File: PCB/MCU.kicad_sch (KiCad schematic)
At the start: 15 parts, among them U1 STM32G431CBT6, Y1 8MHz

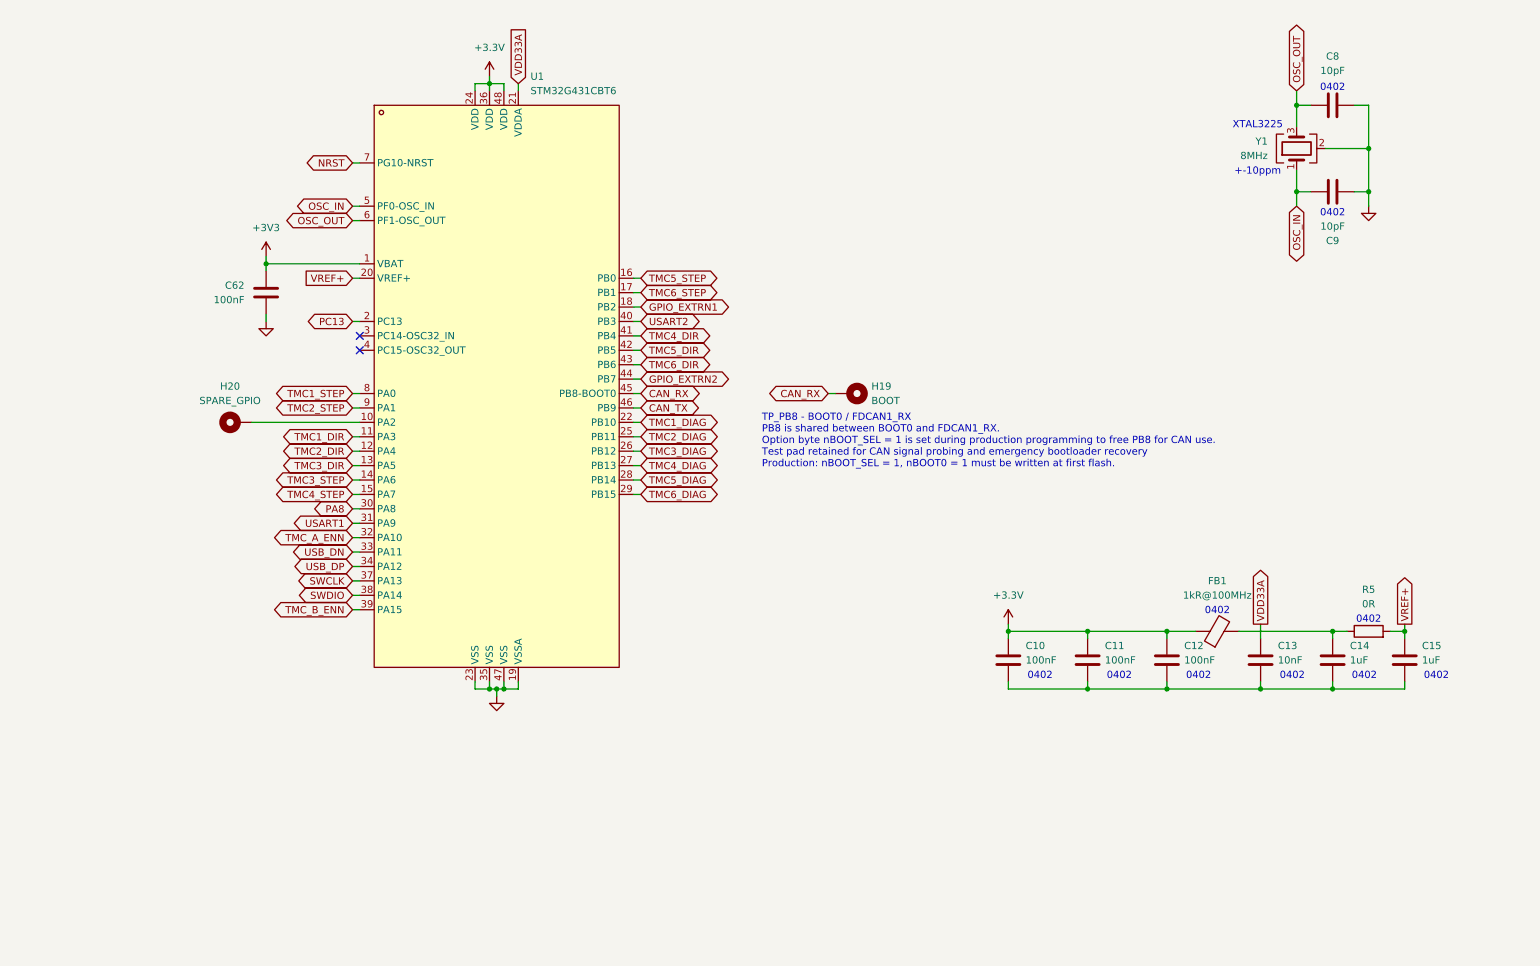
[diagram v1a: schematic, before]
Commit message: Improved Protection and Board Testability - Added power rail protection and decoupling for stepper motor noise environment - Added TVS, bulk caps and fuse upgrade on 24V rail - Added test pads for bring-up and debugging
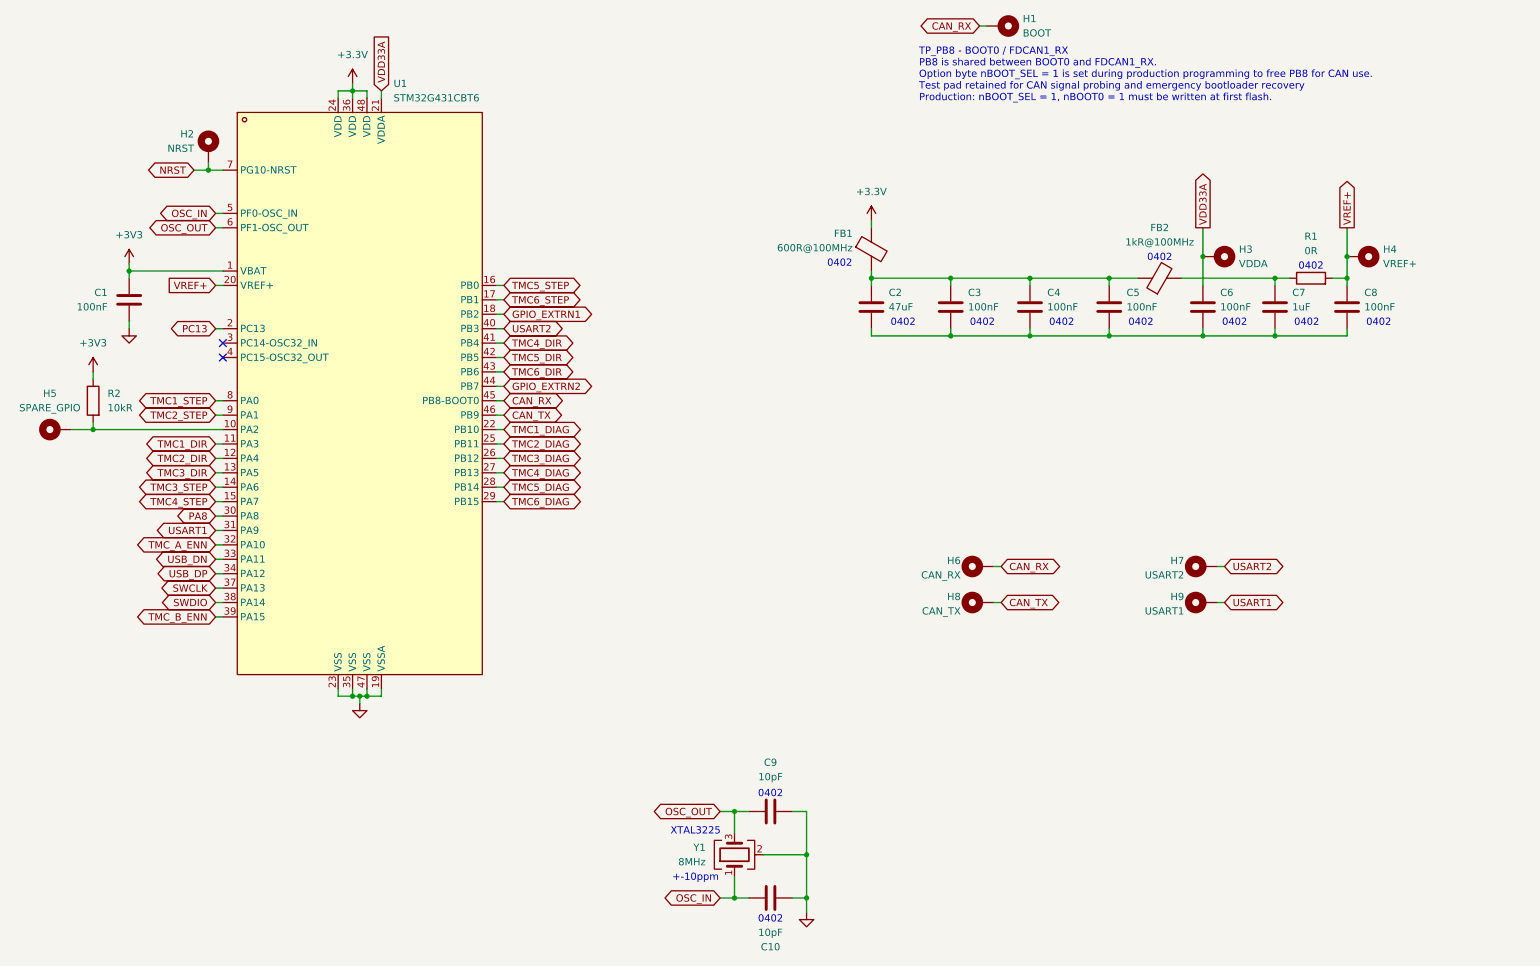
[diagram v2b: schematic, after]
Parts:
- added C2: 47uF, Capacitor_SMD:C_0603_1608Metric, symbol Device:C
- added FB1: 600R@100MHz, Inductor_SMD:L_0402_1005Metric, symbol Device:FerriteBead
- added H2: NRST, TestPoint:TestPoint_Pad_D1.0mm, symbol Mechanical:MountingHole_Pad
- added H3: VDDA, TestPoint:TestPoint_Pad_D2.0mm, symbol Mechanical:MountingHole_Pad
- added H4: VREF+, TestPoint:TestPoint_Pad_D2.0mm, symbol Mechanical:MountingHole_Pad
- added H6: CAN_RX, TestPoint:TestPoint_Pad_D1.0mm, symbol Mechanical:MountingHole_Pad
- added H7: USART2, TestPoint:TestPoint_Pad_D1.0mm, symbol Mechanical:MountingHole_Pad
- added H8: CAN_TX, TestPoint:TestPoint_Pad_D1.0mm, symbol Mechanical:MountingHole_Pad
- added H9: USART1, TestPoint:TestPoint_Pad_D1.0mm, symbol Mechanical:MountingHole_Pad
- added R2: 10kR, Resistor_SMD:R_0402_1005Metric, symbol Device:R
- C6: renamed from C13; value 10nF -> 100nF
- C8: renamed from C15; value 1uF -> 100nF
- H1: renamed from H19; footprint TestPoint:TestPoint_Pad_D1.5mm -> TestPoint:TestPoint_Pad_D1.0mm
- H5: renamed from H20; footprint TestPoint:TestPoint_Pad_D1.5mm -> TestPoint:TestPoint_Pad_D1.0mm
- renumbered C62 to C1, C9 to C10, C10 to C3, C11 to C4, C12 to C5, C14 to C7, C8 to C9, FB1 to FB2, R5 to R1
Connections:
- net +3.3V: now also FB1.1; no longer C3.1, C4.1, C5.1, FB2.1
- net +3V3: now also R2.1
- net CAN_RX: now also H6.1
- net CAN_TX: now also H8.1
- net NRST: now also H2.1
- net USART1: now also H9.1
- net USART2: now also H7.1
- net VDD33A: now also H3.1
- net VREF+: now also H4.1
- net at C3.2, C4.2, C5.2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: now also C2.2
- net at H5.1, U1.10 (PA2): now also R2.2
- new net: C2.1, C3.1, C4.1, C5.1, FB1.2, FB2.1
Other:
- moved on the sheet: C1, C10, C3, C4, C5, C6, C7, C8, C9, FB2, H1, H5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

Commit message: Started laying out the PCB - Decided for a square-shaped board - Split Motor Controllers on top and bottom - Split Power Plane (+3V3 on logic side, +24V on motor side) - Roughly layed out the board entirely - Reconsidered my life choises (got sick)
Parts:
- renumbered C8 to C10, C9 to C2, C10 to C3, C2 to C4, C3 to C5, C4 to C6, C5 to C7, C6 to C8, C7 to C9, H5 to H1, H6 to H3, H8 to H4, H1 to H5, H7 to H6, H9 to H7, H3 to H8, H4 to H9, R2 to R1, R1 to R2
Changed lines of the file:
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@@
 		)
 	)
-	(global_label "TMC1_STEP"
-		(shape bidirectional)
-		(at 54.61 96.52 180)
-		(effects
-			(font
-				(size 1.27 1.27)
-			)
-			(justify right)
-		)
-		(property "Intersheetrefs" "${INTERSHEET_REFS}"
-			(at 54.61 96.52 0)
-			(hide yes)
-			(show_name no)
-			(do_not_autoplace no)
-			(effects
-				(font
-					(size 1.27 1.27)
-				)
-			)
-		)
-	)
 	(global_label "NRST"
 		(shape bidirectional)
@@
 		)
 	)
+	(global_label "TMC1_STEP"
+		(shape bidirectional)
+		(at 54.61 96.52 180)
+		(effects
+			(font
+				(size 1.27 1.27)
+			)
+			(justify right)
+		)
+		(property "Intersheetrefs" "${INTERSHEET_REFS}"
+			(at 54.61 96.52 0)
+			(hide yes)
+			(show_name no)
+			(do_not_autoplace no)
+			(effects
+				(font
+					(size 1.27 1.27)
+				)
+			)
+		)
+	)
 	(global_label "TMC1_DIAG"
 		(shape bidirectional)
@@
 		(in_pos_files yes)
 		(dnp no)
-		(property "Reference" "H8"
+		(property "Reference" "H4"
 			(at 185.928 131.064 90)
 			(show_name no)
@@
 			(project "Arm_Controller"
 				(path "/2323d903-32ae-4da3-a89f-487023e10892/eaca7fd8-f393-449d-a4df-681d2188ea9b"
-					(reference "H8")
+					(reference "H4")
 					(unit 1)
 				)
@@
 		(in_pos_files yes)
 		(dnp no)
-		(property "Reference" "H9"
+		(property "Reference" "H7"
 			(at 225.298 131.064 90)
 			(show_name no)
@@
 			(project "Arm_Controller"
 				(path "/2323d903-32ae-4da3-a89f-487023e10892/eaca7fd8-f393-449d-a4df-681d2188ea9b"
-					(reference "H9")
+					(reference "H7")
 					(unit 1)
 				)
@@
 		(dnp no)
 		(fields_autoplaced yes)
-		(property "Reference" "#PWR02"
+		(property "Reference" "#PWR07"
 			(at 170.18 68.58 0)
 			(hide yes)
@@
 			(project "Arm_Controller"
 				(path "/2323d903-32ae-4da3-a89f-487023e10892/eaca7fd8-f393-449d-a4df-681d2188ea9b"
-					(reference "#PWR02")
+					(reference "#PWR07")
 					(unit 1)
 				)
@@
 		(in_pos_files yes)
 		(dnp no)
-		(property "Reference" "C5"
+		(property "Reference" "C7"
 			(at 215.138 77.47 0)
 			(show_name no)
@@
 			(project "Arm_Controller"
 				(path "/2323d903-32ae-4da3-a89f-487023e10892/eaca7fd8-f393-449d-a4df-681d2188ea9b"
-					(reference "C5")
+					(reference "C7")
 					(unit 1)
 				)
@@
 		(dnp no)
 		(fields_autoplaced yes)
-		(property "Reference" "H5"
+		(property "Reference" "H1"
 			(at 25.4 95.25 90)
 			(show_name no)
@@
 			(project "Arm_Controller"
 				(path "/2323d903-32ae-4da3-a89f-487023e10892/eaca7fd8-f393-449d-a4df-681d2188ea9b"
-					(reference "H5")
+					(reference "H1")
 					(unit 1)
 				)
@@
 		(in_pos_files yes)
 		(dnp no)
-		(property "Reference" "C4"
+		(property "Reference" "C6"
 			(at 201.168 77.47 0)
 			(show_name no)
@@
 			(project "Arm_Controller"
 				(path "/2323d903-32ae-4da3-a89f-487023e10892/eaca7fd8-f393-449d-a4df-681d2188ea9b"
-					(reference "C4")
+					(reference "C6")
 					(unit 1)
 				)
@@
 		(in_pos_files yes)
 		(dnp no)
-		(property "Reference" "C3"
+		(property "Reference" "C5"
 			(at 187.198 77.47 0)
 			(show_name no)
@@
 			(project "Arm_Controller"
 				(path "/2323d903-32ae-4da3-a89f-487023e10892/eaca7fd8-f393-449d-a4df-681d2188ea9b"
-					(reference "C3")
+					(reference "C5")
 					(unit 1)
 				)
@@
 		(in_pos_files yes)
 		(dnp no)
-		(property "Reference" "C10"
+		(property "Reference" "C3"
 			(at 152.4 192.786 90)
 			(show_name no)
@@
 			(project "Arm_Controller"
 				(path "/2323d903-32ae-4da3-a89f-487023e10892/eaca7fd8-f393-449d-a4df-681d2188ea9b"
-					(reference "C10")
+					(reference "C3")
 					(unit 1)
 				)
@@
 		(in_pos_files yes)
 		(dnp no)
-		(property "Reference" "R2"
+		(property "Reference" "R1"
 			(at 35.56 95.2499 0)
 			(show_name no)
@@
 			(project "Arm_Controller"
 				(path "/2323d903-32ae-4da3-a89f-487023e10892/eaca7fd8-f393-449d-a4df-681d2188ea9b"
-					(reference "R2")
+					(reference "R1")
 					(unit 1)
 				)
@@
 		(in_pos_files yes)
 		(dnp no)
-		(property "Reference" "C7"
+		(property "Reference" "C9"
 			(at 244.348 77.47 0)
 			(show_name no)
@@
 			(project "Arm_Controller"
 				(path "/2323d903-32ae-4da3-a89f-487023e10892/eaca7fd8-f393-449d-a4df-681d2188ea9b"
-					(reference "C7")
+					(reference "C9")
 					(unit 1)
 				)
@@
 		(dnp no)
 		(fields_autoplaced yes)
-		(property "Reference" "#PWR06"
+		(property "Reference" "#PWR05"
 			(at 80.01 156.21 0)
 			(hide yes)
@@
 			(project "Arm_Controller"
 				(path "/2323d903-32ae-4da3-a89f-487023e10892/eaca7fd8-f393-449d-a4df-681d2188ea9b"
-					(reference "#PWR06")
+					(reference "#PWR05")
 					(unit 1)
 				)
@@
 		(in_pos_files yes)
 		(dnp no)
-		(property "Reference" "R1"
+		(property "Reference" "R2"
 			(at 247.65 67.564 90)
 			(show_name no)
@@
 			(project "Arm_Controller"
 				(path "/2323d903-32ae-4da3-a89f-487023e10892/eaca7fd8-f393-449d-a4df-681d2188ea9b"
-					(reference "R1")
+					(reference "R2")
 					(unit 1)
 				)
@@
 		(dnp no)
 		(fields_autoplaced yes)
-		(property "Reference" "#PWR07"
+		(property "Reference" "#PWR06"
 			(at 158.75 193.04 0)
 			(hide yes)
@@
 			(project "Arm_Controller"
 				(path "/2323d903-32ae-4da3-a89f-487023e10892/eaca7fd8-f393-449d-a4df-681d2188ea9b"
-					(reference "#PWR07")
+					(reference "#PWR06")
 					(unit 1)
 				)
@@
 		(in_pos_files yes)
 		(dnp no)
-		(property "Reference" "C6"
+		(property "Reference" "C8"
 			(at 231.648 77.47 0)
 			(show_name no)
@@
 			(project "Arm_Controller"
 				(path "/2323d903-32ae-4da3-a89f-487023e10892/eaca7fd8-f393-449d-a4df-681d2188ea9b"
-					(reference "C6")
+					(reference "C8")
 					(unit 1)
 				)
@@
 		(in_pos_files yes)
 		(dnp no)
-		(property "Reference" "H7"
+		(property "Reference" "H6"
 			(at 225.298 124.714 90)
 			(show_name no)
@@
 			(project "Arm_Controller"
 				(path "/2323d903-32ae-4da3-a89f-487023e10892/eaca7fd8-f393-449d-a4df-681d2188ea9b"
-					(reference "H7")
+					(reference "H6")
 					(unit 1)
 				)
@@
 		(in_pos_files yes)
 		(dnp no)
-		(property "Reference" "C2"
+		(property "Reference" "C4"
 			(at 173.228 77.47 0)
 			(show_name no)
@@
 			(project "Arm_Controller"
 				(path "/2323d903-32ae-4da3-a89f-487023e10892/eaca7fd8-f393-449d-a4df-681d2188ea9b"
-					(reference "C2")
+					(reference "C4")
 					(unit 1)
 				)
@@
 		(dnp no)
 		(fields_autoplaced yes)
-		(property "Reference" "#PWR03"
+		(property "Reference" "#PWR02"
 			(at 39.37 76.2 0)
 			(hide yes)
@@
 			(project "Arm_Controller"
 				(path "/2323d903-32ae-4da3-a89f-487023e10892/eaca7fd8-f393-449d-a4df-681d2188ea9b"
-					(reference "#PWR03")
+					(reference "#PWR02")
 					(unit 1)
 				)
@@
 		(dnp no)
 		(fields_autoplaced yes)
-		(property "Reference" "#PWR05"
+		(property "Reference" "#PWR01"
 			(at 33.02 95.25 0)
 			(hide yes)
@@
 			(project "Arm_Controller"
 				(path "/2323d903-32ae-4da3-a89f-487023e10892/eaca7fd8-f393-449d-a4df-681d2188ea9b"
-					(reference "#PWR05")
+					(reference "#PWR01")
 					(unit 1)
 				)
@@
 		(dnp no)
 		(fields_autoplaced yes)
-		(property "Reference" "H1"
+		(property "Reference" "H5"
 			(at 196.85 29.2099 90)
 			(show_name no)
@@
 			(project "Arm_Controller"
 				(path "/2323d903-32ae-4da3-a89f-487023e10892/eaca7fd8-f393-449d-a4df-681d2188ea9b"
-					(reference "H1")
+					(reference "H5")
 					(unit 1)
 				)
@@
 		(in_pos_files yes)
 		(dnp no)
-		(property "Reference" "H6"
+		(property "Reference" "H3"
 			(at 185.928 124.714 90)
 			(show_name no)
@@
 			(project "Arm_Controller"
 				(path "/2323d903-32ae-4da3-a89f-487023e10892/eaca7fd8-f393-449d-a4df-681d2188ea9b"
-					(reference "H6")
+					(reference "H3")
 					(unit 1)
 				)
@@
 		(dnp no)
 		(fields_autoplaced yes)
-		(property "Reference" "H3"
+		(property "Reference" "H8"
 			(at 234.95 69.8499 90)
 			(show_name no)
@@
 			(project "Arm_Controller"
 				(path "/2323d903-32ae-4da3-a89f-487023e10892/eaca7fd8-f393-449d-a4df-681d2188ea9b"
-					(reference "H3")
+					(reference "H8")
 					(unit 1)
 				)
@@
 		(in_pos_files yes)
 		(dnp no)
-		(property "Reference" "C9"
+		(property "Reference" "C2"
 			(at 152.4 160.274 90)
 			(show_name no)
@@
 			(project "Arm_Controller"
 				(path "/2323d903-32ae-4da3-a89f-487023e10892/eaca7fd8-f393-449d-a4df-681d2188ea9b"
-					(reference "C9")
+					(reference "C2")
 					(unit 1)
 				)
@@
 		(dnp no)
 		(fields_autoplaced yes)
-		(property "Reference" "#PWR04"
+		(property "Reference" "#PWR03"
 			(at 39.37 90.17 0)
 			(hide yes)
@@
 			(project "Arm_Controller"
 				(path "/2323d903-32ae-4da3-a89f-487023e10892/eaca7fd8-f393-449d-a4df-681d2188ea9b"
-					(reference "#PWR04")
+					(reference "#PWR03")
 					(unit 1)
 				)
@@
 		(in_pos_files yes)
 		(dnp no)
-		(property "Reference" "C8"
+		(property "Reference" "C10"
 			(at 257.048 77.47 0)
 			(show_name no)
@@
 			(project "Arm_Controller"
 				(path "/2323d903-32ae-4da3-a89f-487023e10892/eaca7fd8-f393-449d-a4df-681d2188ea9b"
-					(reference "C8")
+					(reference "C10")
 					(unit 1)
 				)
@@
 		(dnp no)
 		(fields_autoplaced yes)
-		(property "Reference" "#PWR01"
+		(property "Reference" "#PWR04"
 			(at 78.74 44.45 0)
 			(hide yes)
@@
 			(project "Arm_Controller"
 				(path "/2323d903-32ae-4da3-a89f-487023e10892/eaca7fd8-f393-449d-a4df-681d2188ea9b"
-					(reference "#PWR01")
+					(reference "#PWR04")
 					(unit 1)
 				)
@@
 		(dnp no)
 		(fields_autoplaced yes)
-		(property "Reference" "H4"
+		(property "Reference" "H9"
 			(at 260.35 69.8499 90)
 			(show_name no)
@@
 			(project "Arm_Controller"
 				(path "/2323d903-32ae-4da3-a89f-487023e10892/eaca7fd8-f393-449d-a4df-681d2188ea9b"
-					(reference "H4")
+					(reference "H9")
 					(unit 1)
 				)
